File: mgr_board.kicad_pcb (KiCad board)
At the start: 2 copper layers, 150 x 150 mm, 239 parts, among them IC1 MCP48CVB08-20E_ST, IC10 A6214KLKTR-T, IC11 A6214KLKTR-T, IC12 A6214KLKTR-T, IC13 A6214KLKTR-T, IC2 A6214KLKTR-T, IC3 A6214KLKTR-T, IC4 A6214KLKTR-T, IC5 A6214KLKTR-T, IC6 A6214KLKTR-T, IC7 A6214KLKTR-T, IC8 A6214KLKTR-T, IC9 A6214KLKTR-T, J1 Screw_Terminal_2_P5.00mm, J3 SD Card SPI Module, J4 Micro_SD_Card, U1 TPS562201DDCR, U2 LM2596 BUCK MODULE

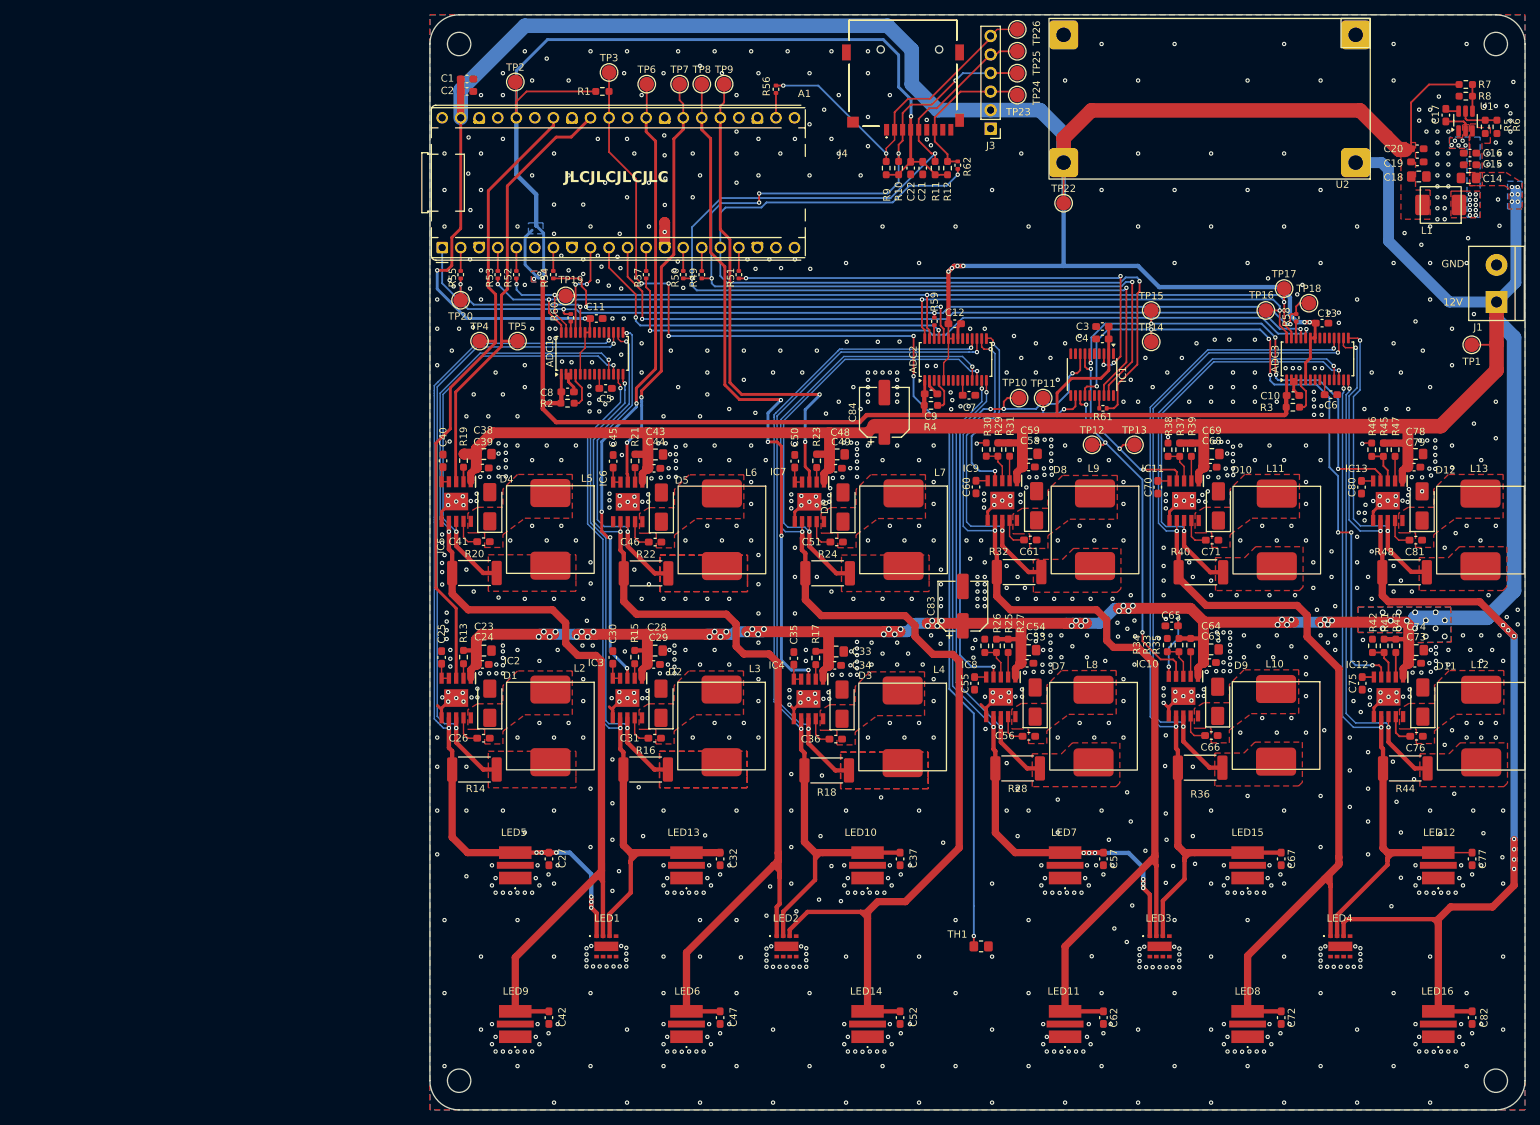
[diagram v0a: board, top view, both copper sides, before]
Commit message: Added current sense amplifier, reduced one ADC, changed elec cap to tantals, to review
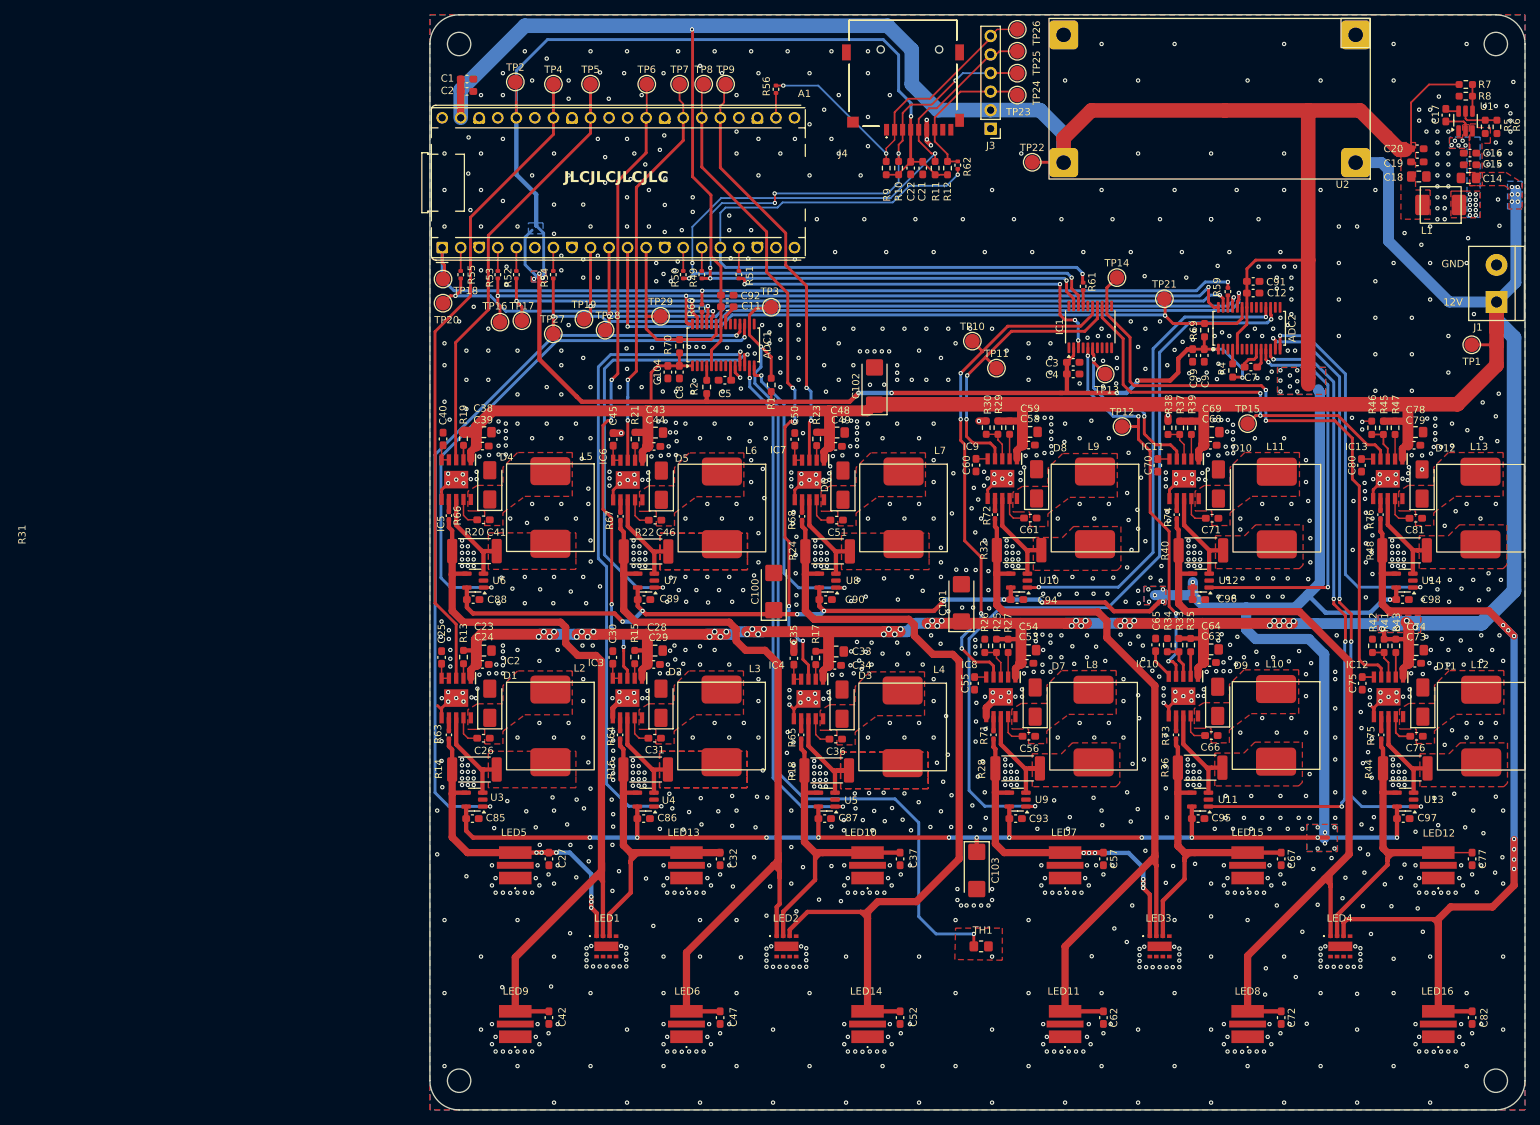
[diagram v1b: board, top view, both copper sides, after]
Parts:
- removed ADC3: ADS1148QPWRQ1, Package_SO:TSSOP-28_4.4x9.7mm_P0.65mm
- removed C10, C13: 100nF, Capacitor_SMD:C_0603_1608Metric_Pad1.08x0.95mm_HandSolder
- removed C6: 1uF, Capacitor_SMD:C_0603_1608Metric_Pad1.08x0.95mm_HandSolder
- removed C83, C84: 100uF, Capacitor_SMD:CP_Elec_6.3x7.7
- removed R3: 10k, Resistor_SMD:R_0603_1608Metric_Pad0.98x0.95mm_HandSolder
- removed R57, R58: NMT, Resistor_SMD:R_0402_1005Metric
- added C100: 47uF, Capacitor_Tantalum_SMD:CP_EIA-6032-15_Kemet-U_Pad2.25x2.35mm_HandSolder, F.Cu at (65.1, 100.0)
- added C101: 47uF, Capacitor_Tantalum_SMD:CP_EIA-6032-15_Kemet-U_Pad2.25x2.35mm_HandSolder, F.Cu at (90.8, 101.5)
- added C102: 47uF, Capacitor_Tantalum_SMD:CP_EIA-6032-15_Kemet-U_Pad2.25x2.35mm_HandSolder, F.Cu at (78.9, 71.8)
- added C103: 47uF, Capacitor_Tantalum_SMD:CP_EIA-6032-15_Kemet-U_Pad2.25x2.35mm_HandSolder, F.Cu at (92.9, 138.2)
- added C104: 4,7uF, Capacitor_SMD:C_0603_1608Metric_Pad1.08x0.95mm_HandSolder, F.Cu at (50.6, 69.9)
- added C85: 100nF, Capacitor_SMD:C_0603_1608Metric_Pad1.08x0.95mm_HandSolder, F.Cu at (23.8, 131.1)
- added C86: 100nF, Capacitor_SMD:C_0603_1608Metric_Pad1.08x0.95mm_HandSolder, F.Cu at (47.3, 131.1)
- added C87: 100nF, Capacitor_SMD:C_0603_1608Metric_Pad1.08x0.95mm_HandSolder, F.Cu at (72.1, 131.1)
- added C88: 100nF, Capacitor_SMD:C_0603_1608Metric_Pad1.08x0.95mm_HandSolder, F.Cu at (23.9, 101.1)
- added C89: 100nF, Capacitor_SMD:C_0603_1608Metric_Pad1.08x0.95mm_HandSolder, F.Cu at (47.3, 101.1)
- added C90: 100nF, Capacitor_SMD:C_0603_1608Metric_Pad1.08x0.95mm_HandSolder, F.Cu at (72.2, 101.1)
- added C91: 4,7uF, Capacitor_SMD:C_0603_1608Metric_Pad1.08x0.95mm_HandSolder, F.Cu at (130.8, 57.5)
- added C92: 4,7uF, Capacitor_SMD:C_0603_1608Metric_Pad1.08x0.95mm_HandSolder, F.Cu at (58.7, 59.4)
- added C93: 100nF, Capacitor_SMD:C_0603_1608Metric_Pad1.08x0.95mm_HandSolder, F.Cu at (98.2, 131.1)
- added C94: 100nF, Capacitor_SMD:C_0603_1608Metric_Pad1.08x0.95mm_HandSolder, F.Cu at (98.4, 101.1)
- added C95: 100nF, Capacitor_SMD:C_0603_1608Metric_Pad1.08x0.95mm_HandSolder, F.Cu at (123.2, 131.1)
- added C96: 100nF, Capacitor_SMD:C_0603_1608Metric_Pad1.08x0.95mm_HandSolder, F.Cu at (123.3, 101.1)
- added C97: 100nF, Capacitor_SMD:C_0603_1608Metric_Pad1.08x0.95mm_HandSolder, F.Cu at (151.3, 131.1)
- added C98: 100nF, Capacitor_SMD:C_0603_1608Metric_Pad1.08x0.95mm_HandSolder, F.Cu at (151.2, 101.1)
- added C99: 4,7uF, Capacitor_SMD:C_0603_1608Metric_Pad1.08x0.95mm_HandSolder, F.Cu at (122.5, 67.7)
- added R63: 0R, Capacitor_SMD:C_0402_1005Metric_Pad0.74x0.62mm_HandSolder, F.Cu at (20.6, 119.6)
- added R64: 0R, Capacitor_SMD:C_0402_1005Metric_Pad0.74x0.62mm_HandSolder, F.Cu at (44.0, 119.6)
- added R65: 0R, Capacitor_SMD:C_0402_1005Metric_Pad0.74x0.62mm_HandSolder, F.Cu at (68.8, 119.6)
- added R66: 0R, Capacitor_SMD:C_0402_1005Metric_Pad0.74x0.62mm_HandSolder, F.Cu at (20.6, 89.6)
- added R67: 0R, Capacitor_SMD:C_0402_1005Metric_Pad0.74x0.62mm_HandSolder, F.Cu at (44.1, 89.7)
- added R68: 0R, Capacitor_SMD:C_0402_1005Metric_Pad0.74x0.62mm_HandSolder, F.Cu at (69.0, 89.7)
- added R69: 10k, Resistor_SMD:R_0603_1608Metric_Pad0.98x0.95mm_HandSolder, F.Cu at (124.1, 64.2)
- added R70: 10k, Resistor_SMD:R_0603_1608Metric_Pad0.98x0.95mm_HandSolder, F.Cu at (52.2, 66.4)
- added R71: 0R, Capacitor_SMD:C_0402_1005Metric_Pad0.74x0.62mm_HandSolder, F.Cu at (95.2, 119.6)
- added R72: 0R, Capacitor_SMD:C_0402_1005Metric_Pad0.74x0.62mm_HandSolder, F.Cu at (95.4, 89.5)
- added R73: 0R, Capacitor_SMD:C_0402_1005Metric_Pad0.74x0.62mm_HandSolder, F.Cu at (120.2, 119.6)
- added R74: 0R, Capacitor_SMD:C_0402_1005Metric_Pad0.74x0.62mm_HandSolder, F.Cu at (120.3, 89.5)
- added R75: 0R, Capacitor_SMD:C_0402_1005Metric_Pad0.74x0.62mm_HandSolder, F.Cu at (148.3, 119.6)
- added R76: 0R, Capacitor_SMD:C_0402_1005Metric_Pad0.74x0.62mm_HandSolder, F.Cu at (148.2, 89.5)
- added TP21: TestPoint, TestPoint:TestPoint_Pad_D2.0mm, F.Cu at (118.6, 59.9)
- added TP27: TestPoint, TestPoint:TestPoint_Pad_D2.0mm, F.Cu at (34.9, 64.7)
- added TP28: TestPoint, TestPoint:TestPoint_Pad_D2.0mm, F.Cu at (42.0, 64.2)
- added TP29: TestPoint, TestPoint:TestPoint_Pad_D2.0mm, F.Cu at (49.6, 62.3)
- added U10: INA180A1, Package_TO_SOT_SMD:SOT-23-5, F.Cu at (98.7, 98.5)
- added U11: INA180A1, Package_TO_SOT_SMD:SOT-23-5, F.Cu at (123.5, 128.5)
- added U12: INA180A1, Package_TO_SOT_SMD:SOT-23-5, F.Cu at (123.6, 98.5)
- added U13: INA180A1, Package_TO_SOT_SMD:SOT-23-5, F.Cu at (151.6, 128.5)
- added U14: INA180A1, Package_TO_SOT_SMD:SOT-23-5, F.Cu at (151.5, 98.5)
- added U3: INA180A1, Package_TO_SOT_SMD:SOT-23-5, F.Cu at (24.1, 128.5)
- added U4: INA180A1, Package_TO_SOT_SMD:SOT-23-5, F.Cu at (47.5, 128.5)
- added U5: INA180A1, Package_TO_SOT_SMD:SOT-23-5, F.Cu at (72.3, 128.5)
- added U6: INA180A1, Package_TO_SOT_SMD:SOT-23-5, F.Cu at (24.2, 98.5)
- added U7: INA180A1, Package_TO_SOT_SMD:SOT-23-5, F.Cu at (47.6, 98.5)
- added U8: INA180A1, Package_TO_SOT_SMD:SOT-23-5, F.Cu at (72.5, 98.5)
- added U9: INA180A1, Package_TO_SOT_SMD:SOT-23-5, F.Cu at (98.5, 128.5)
- R14, R16, R18, R20, R22, R24: value R120 or R260 -> R150 or R250
- R28, R32, R36, R40, R44, R48: value R120 or R260 -> R180 or R250
- moved TP18 118.6 mm to (19.8, 57.2)
- moved TP16 104.9 mm to (27.6, 63.1)
- moved TP17 104.5 mm to (30.6, 62.9)
- moved R1 46.4 mm to (64.8, 71.7), turned to -90 degrees
- moved R4 41.6 mm to (128.0, 69.7), turned to -90 degrees
- moved C12 41.1 mm to (130.8, 59.1)
- moved ADC2 40.5 mm to (130.2, 63.9)
- moved R59 40.4 mm to (127.3, 58.9)
- moved TP3 39.1 mm to (64.8, 61.0)
- moved C7 38.8 mm to (130.4, 69.2)
- moved C9 37.8 mm to (124.1, 67.7), turned to -90 degrees
- moved TP4 36.6 mm to (34.9, 30.5)
- moved TP5 36.6 mm to (40.0, 30.5)
- moved TP15 20.4 mm to (130.0, 77.0)
- moved R2 19.2 mm to (55.9, 72.0), turned to -90 degrees
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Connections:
- net /I_LED_10 renamed Net-(IC12-CSH)
- net /I_LED_11 renamed Net-(IC13-CSH)
- net /I_LED_8 renamed Net-(IC10-CSH)
- net /I_LED_9 renamed Net-(IC11-CSH)
- A1 pad 11: /ADC2_DRDY -> /ADC1_START
- A1 pad 12: Net-(A1-GP9) -> /ADC0_START
- A1 pad 31: /ADC_NTC -> unconnected-(A1-ADC0/GP26-Pad31)
- ADC1 pad 11: /LED_1 -> /ADCs/LED_CURR_2
- ADC1 pad 12: /I_LED_1 -> /ADCs/LED_CURR_3
- ADC1 pad 13: /LED_2 -> /ADCs/LED_CURR_4
- ADC1 pad 14: /I_LED_2 -> /ADCs/LED_CURR_5
- ADC1 pad 15: /I_LED_3 -> unconnected-(ADC1-AIN6/IEXC/GPIO6-Pad15)
- ADC1 pad 16: /LED_3 -> /ADC_NTC
- ADC1 pad 17: /I_LED_0 -> /ADCs/LED_CURR_1
- ADC1 pad 18: /LED_0 -> /ADCs/LED_CURR_0
- ADC1 pad 23: +5V -> /ADC0_START
- ADC2 pad 11: /LED_5 -> /ADCs/LED_CURR_9
- ADC2 pad 12: /I_LED_5 -> /ADCs/LED_CURR_8
- ADC2 pad 13: /LED_6 -> /ADCs/LED_CURR_10
- ADC2 pad 14: /I_LED_6 -> /ADCs/LED_CURR_11
- ADC2 pad 15: /I_LED_7 -> unconnected-(ADC2-AIN6/IEXC/GPIO6-Pad15)
- ADC2 pad 16: /LED_7 -> unconnected-(ADC2-AIN7/IEXC/GPIO7-Pad16)
- ADC2 pad 17: /I_LED_4 -> /ADCs/LED_CURR_6
- ADC2 pad 18: /LED_4 -> /ADCs/LED_CURR_7
- ADC2 pad 23: +5V -> /ADC1_START
- C27 pad 1: /LED_0 -> /LED_LOAD_0
- C32 pad 1: /LED_2 -> /LED_LOAD_2
- C37 pad 1: /LED_4 -> /LED_LOAD_4
- C42 pad 1: /LED_1 -> /LED_LOAD_1
- C47 pad 1: /LED_3 -> /LED_LOAD_3
- C52 pad 1: /LED_5 -> /LED_LOAD_5
- C57 pad 1: /LED_6 -> /LED_LOAD_6
- C62 pad 1: /LED_7 -> /LED_LOAD_7
- C67 pad 1: /LED_8 -> /LED_LOAD_8
- C72 pad 1: /LED_9 -> /LED_LOAD_9
- C77 pad 1: /LED_10 -> /LED_LOAD_10
- C82 pad 1: /LED_11 -> /LED_LOAD_11
- IC1 pad 12: /ADIM_1 -> /ADIM_4
- IC1 pad 13: /ADIM_2 -> /ADIM_5
- IC1 pad 14: /ADIM_4 -> /ADIM_1
- IC1 pad 15: /ADIM_7 -> /ADIM_0
- IC1 pad 5: /ADIM_6 -> /ADIM_2
- IC1 pad 6: /ADIM_5 -> /ADIM_3
- IC1 pad 7: /ADIM_3 -> unconnected-(IC1-VOUT4-Pad7)
- IC1 pad 8: /ADIM_0 -> unconnected-(IC1-VOUT6-Pad8)
- IC10 pad 7: /LED_8 -> Net-(IC10-CSL)
- IC11 pad 7: /LED_9 -> Net-(IC11-CSL)
- IC12 pad 7: /LED_10 -> Net-(IC12-CSL)
- IC13 pad 7: /LED_11 -> Net-(IC13-CSL)
- IC2 pad 7: /LED_0 -> Net-(IC2-CSL)
- IC2 pad 8: /I_LED_0 -> Net-(IC2-CSH)
- IC3 pad 7: /LED_2 -> Net-(IC3-CSL)
- IC3 pad 8: /I_LED_2 -> Net-(IC3-CSH)
- IC4 pad 7: /LED_4 -> Net-(IC4-CSL)
- IC4 pad 8: /I_LED_4 -> Net-(IC4-CSH)
- IC5 pad 7: /LED_1 -> Net-(IC5-CSL)
- IC5 pad 8: /I_LED_1 -> Net-(IC5-CSH)
- IC6 pad 7: /LED_3 -> Net-(IC6-CSL)
- IC6 pad 8: /I_LED_3 -> Net-(IC6-CSH)
- IC7 pad 7: /LED_5 -> Net-(IC7-CSL)
- IC7 pad 8: /I_LED_5 -> Net-(IC7-CSH)
- IC8 pad 7: /LED_6 -> Net-(IC8-CSL)
- IC8 pad 8: /I_LED_6 -> Net-(IC8-CSH)
- IC9 pad 7: /LED_7 -> Net-(IC9-CSL)
- IC9 pad 8: /I_LED_7 -> Net-(IC9-CSH)
- L2 pad 2: /I_LED_0 -> Net-(IC2-CSH)
- L3 pad 2: /I_LED_2 -> Net-(IC3-CSH)
- L4 pad 2: /I_LED_4 -> Net-(IC4-CSH)
- L5 pad 2: /I_LED_1 -> Net-(IC5-CSH)
- L6 pad 2: /I_LED_3 -> Net-(IC6-CSH)
- L7 pad 2: /I_LED_5 -> Net-(IC7-CSH)
- L8 pad 2: /I_LED_6 -> Net-(IC8-CSH)
- L9 pad 2: /I_LED_7 -> Net-(IC9-CSH)
- LED1 pad 1: /LED_0 -> /LED_LOAD_0
- LED1 pad 2: /LED_1 -> /LED_LOAD_1
- LED1 pad 3: /LED_2 -> /LED_LOAD_2
- LED10 pad 2: /LED_4 -> /LED_LOAD_4
- LED11 pad 2: /LED_7 -> /LED_LOAD_7
- LED12 pad 2: /LED_10 -> /LED_LOAD_10
- LED13 pad 2: /LED_2 -> /LED_LOAD_2
- LED14 pad 2: /LED_5 -> /LED_LOAD_5
- LED15 pad 2: /LED_8 -> /LED_LOAD_8
- LED16 pad 2: /LED_11 -> /LED_LOAD_11
- LED2 pad 1: /LED_3 -> /LED_LOAD_3
- LED2 pad 2: /LED_4 -> /LED_LOAD_4
- LED2 pad 3: /LED_5 -> /LED_LOAD_5
- LED3 pad 1: /LED_6 -> /LED_LOAD_6
- LED3 pad 2: /LED_7 -> /LED_LOAD_7
- LED3 pad 3: /LED_8 -> /LED_LOAD_8
- LED4 pad 1: /LED_9 -> /LED_LOAD_9
- LED4 pad 2: /LED_10 -> /LED_LOAD_10
- LED4 pad 3: /LED_11 -> /LED_LOAD_11
- LED5 pad 2: /LED_0 -> /LED_LOAD_0
- LED6 pad 2: /LED_3 -> /LED_LOAD_3
- LED7 pad 2: /LED_6 -> /LED_LOAD_6
- LED8 pad 2: /LED_9 -> /LED_LOAD_9
- LED9 pad 2: /LED_1 -> /LED_LOAD_1
- R14 pad 1: /LED_0 -> /LED_LOAD_0
- R14 pad 2: /I_LED_0 -> Net-(IC2-CSH)
- R16 pad 1: /LED_2 -> /LED_LOAD_2
- R16 pad 2: /I_LED_2 -> Net-(IC3-CSH)
- R18 pad 1: /LED_4 -> /LED_LOAD_4
- R18 pad 2: /I_LED_4 -> Net-(IC4-CSH)
- R20 pad 1: /LED_1 -> /LED_LOAD_1
- R20 pad 2: /I_LED_1 -> Net-(IC5-CSH)
- R22 pad 1: /LED_3 -> /LED_LOAD_3
- R22 pad 2: /I_LED_3 -> Net-(IC6-CSH)
- R24 pad 1: /LED_5 -> /LED_LOAD_5
- R24 pad 2: /I_LED_5 -> Net-(IC7-CSH)
- R28 pad 1: /LED_6 -> /LED_LOAD_6
- R28 pad 2: /I_LED_6 -> Net-(IC8-CSH)
- R32 pad 1: /LED_7 -> /LED_LOAD_7
- R32 pad 2: /I_LED_7 -> Net-(IC9-CSH)
- R36 pad 1: /LED_8 -> /LED_LOAD_8
- R40 pad 1: /LED_9 -> /LED_LOAD_9
- R44 pad 1: /LED_10 -> /LED_LOAD_10
- R48 pad 1: /LED_11 -> /LED_LOAD_11
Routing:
- net +5V: track 335.3 -> 663.5 mm, vias 8 -> 40
- net /LED_5: track 159.3 -> 0.00 mm, vias 2 -> 0
- net /LED_9: track 152.6 -> 0.00 mm, vias 2 -> 0
- net /LED_1: track 150.9 -> 0.00 mm, vias 2 -> 0
- net /LED_11: track 148.9 -> 0.00 mm, vias 9 -> 0
- net /LED_7: track 142.2 -> 0.00 mm, vias 2 -> 0
- net /LED_3: track 140.8 -> 0.00 mm, vias 2 -> 0
- net /LED_0: track 127.1 -> 0.00 mm, vias 8 -> 0
- net /LED_4: track 123.5 -> 0.00 mm, vias 2 -> 0
- net /LED_8: track 122.9 -> 0.00 mm, vias 2 -> 0
- net /LED_LOAD_11: track 0.00 -> 119.9 mm, vias 0 -> 7
- net /LED_LOAD_5: track 0.00 -> 113.9 mm
- net /LED_LOAD_9: track 0.00 -> 110.7 mm
- net /LED_LOAD_3: track 0.00 -> 110.5 mm
- net /ADCs/LED_CURR_6: track 0.00 -> 109.5 mm, vias 0 -> 2
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- added copper zone on B.Cu, net +5V
- added copper zone on F.Cu, net Net-(IC2-CSH)
- added copper zone on F.Cu, net Net-(IC3-CSH)
- added copper zone on F.Cu, net Net-(IC4-CSH)
- added copper zone on F.Cu, net Net-(IC5-CSH)
- added copper zone on F.Cu, net Net-(IC6-CSH)
- added copper zone on F.Cu, net Net-(IC7-CSH)
- added copper zone on F.Cu, net Net-(IC8-CSH)
- added copper zone on F.Cu, net Net-(IC9-CSH)
- removed copper zone on F.Cu, net /I_LED_0
- removed copper zone on F.Cu, net /I_LED_1
- removed copper zone on F.Cu, net /I_LED_2
- removed copper zone on F.Cu, net /I_LED_3
- removed copper zone on F.Cu, net /I_LED_4
- removed copper zone on F.Cu, net /I_LED_5
- removed copper zone on F.Cu, net /I_LED_6
- removed copper zone on F.Cu, net /I_LED_7
